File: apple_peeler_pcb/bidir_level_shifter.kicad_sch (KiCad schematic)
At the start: 3 parts, among them Q1 2N7002

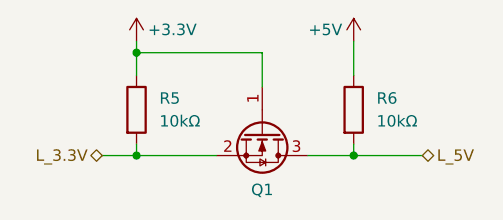
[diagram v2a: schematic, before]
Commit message: replace fancy debug connectors by pin header to save $8
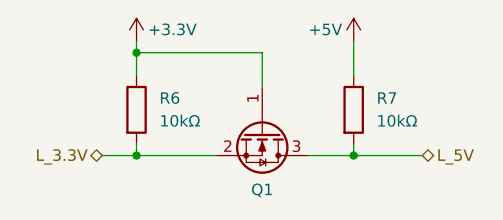
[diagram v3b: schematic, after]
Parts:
- renumbered R5 to R6, R6 to R7
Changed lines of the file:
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@@
 		(dnp no)
 		(fields_autoplaced yes)
-		(property "Reference" "R5"
+		(property "Reference" "R6"
 			(at 146.05 102.8699 0)
 			(effects
@@
 			(project "apple_peeler_pcb"
 				(path "/d5946b96-44a8-4a28-8641-19803e1510af/ab4760da-4146-4688-a275-418314974b55/6e2f9ad3-6df3-44ff-a556-d7733fb95645"
-					(reference "R7")
+					(reference "R8")
 					(unit 1)
 				)
 				(path "/d5946b96-44a8-4a28-8641-19803e1510af/ab4760da-4146-4688-a275-418314974b55/c11db6ac-c72c-4793-88d9-dc045557e97a"
-					(reference "R5")
+					(reference "R6")
 					(unit 1)
 				)
 				(path "/d5946b96-44a8-4a28-8641-19803e1510af/ab4760da-4146-4688-a275-418314974b55/c844b638-b828-4199-a808-926ce8acdcee"
-					(reference "R11")
+					(reference "R12")
 					(unit 1)
 				)
 				(path "/d5946b96-44a8-4a28-8641-19803e1510af/ab4760da-4146-4688-a275-418314974b55/ca35da65-fde1-4d0a-a76e-5585ef239d40"
-					(reference "R9")
+					(reference "R10")
 					(unit 1)
 				)
@@
 		(on_board yes)
 		(dnp no)
-		(property "Reference" "#PWR030"
+		(property "Reference" "#PWR029"
 			(at 167.64 100.33 0)
 			(effects
@@
 			(project "apple_peeler_pcb"
 				(path "/d5946b96-44a8-4a28-8641-19803e1510af/ab4760da-4146-4688-a275-418314974b55/6e2f9ad3-6df3-44ff-a556-d7733fb95645"
-					(reference "#PWR032")
+					(reference "#PWR031")
 					(unit 1)
 				)
 				(path "/d5946b96-44a8-4a28-8641-19803e1510af/ab4760da-4146-4688-a275-418314974b55/c11db6ac-c72c-4793-88d9-dc045557e97a"
-					(reference "#PWR030")
+					(reference "#PWR029")
 					(unit 1)
 				)
 				(path "/d5946b96-44a8-4a28-8641-19803e1510af/ab4760da-4146-4688-a275-418314974b55/c844b638-b828-4199-a808-926ce8acdcee"
-					(reference "#PWR036")
+					(reference "#PWR035")
 					(unit 1)
 				)
 				(path "/d5946b96-44a8-4a28-8641-19803e1510af/ab4760da-4146-4688-a275-418314974b55/ca35da65-fde1-4d0a-a76e-5585ef239d40"
-					(reference "#PWR034")
+					(reference "#PWR033")
 					(unit 1)
 				)
@@
 		(dnp no)
 		(fields_autoplaced yes)
-		(property "Reference" "R6"
+		(property "Reference" "R7"
 			(at 170.18 102.8699 0)
 			(effects
@@
 			(project "apple_peeler_pcb"
 				(path "/d5946b96-44a8-4a28-8641-19803e1510af/ab4760da-4146-4688-a275-418314974b55/6e2f9ad3-6df3-44ff-a556-d7733fb95645"
-					(reference "R8")
+					(reference "R9")
 					(unit 1)
 				)
 				(path "/d5946b96-44a8-4a28-8641-19803e1510af/ab4760da-4146-4688-a275-418314974b55/c11db6ac-c72c-4793-88d9-dc045557e97a"
-					(reference "R6")
+					(reference "R7")
 					(unit 1)
 				)
 				(path "/d5946b96-44a8-4a28-8641-19803e1510af/ab4760da-4146-4688-a275-418314974b55/c844b638-b828-4199-a808-926ce8acdcee"
-					(reference "R12")
+					(reference "R13")
 					(unit 1)
 				)
 				(path "/d5946b96-44a8-4a28-8641-19803e1510af/ab4760da-4146-4688-a275-418314974b55/ca35da65-fde1-4d0a-a76e-5585ef239d40"
-					(reference "R10")
+					(reference "R11")
 					(unit 1)
 				)
@@
 		(on_board yes)
 		(dnp no)
-		(property "Reference" "#PWR029"
+		(property "Reference" "#PWR028"
 			(at 143.51 100.33 0)
 			(effects
@@
 			(project "apple_peeler_pcb"
 				(path "/d5946b96-44a8-4a28-8641-19803e1510af/ab4760da-4146-4688-a275-418314974b55/6e2f9ad3-6df3-44ff-a556-d7733fb95645"
-					(reference "#PWR031")
+					(reference "#PWR030")
 					(unit 1)
 				)
 				(path "/d5946b96-44a8-4a28-8641-19803e1510af/ab4760da-4146-4688-a275-418314974b55/c11db6ac-c72c-4793-88d9-dc045557e97a"
-					(reference "#PWR029")
+					(reference "#PWR028")
 					(unit 1)
 				)
 				(path "/d5946b96-44a8-4a28-8641-19803e1510af/ab4760da-4146-4688-a275-418314974b55/c844b638-b828-4199-a808-926ce8acdcee"
-					(reference "#PWR035")
+					(reference "#PWR034")
 					(unit 1)
 				)
 				(path "/d5946b96-44a8-4a28-8641-19803e1510af/ab4760da-4146-4688-a275-418314974b55/ca35da65-fde1-4d0a-a76e-5585ef239d40"
-					(reference "#PWR033")
-					(unit 1)
-				)
+					(reference "#PWR032")
+					(unit 1)
+				)
